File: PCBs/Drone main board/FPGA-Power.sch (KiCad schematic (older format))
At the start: 45 parts, among them U1201 10CL040_F484

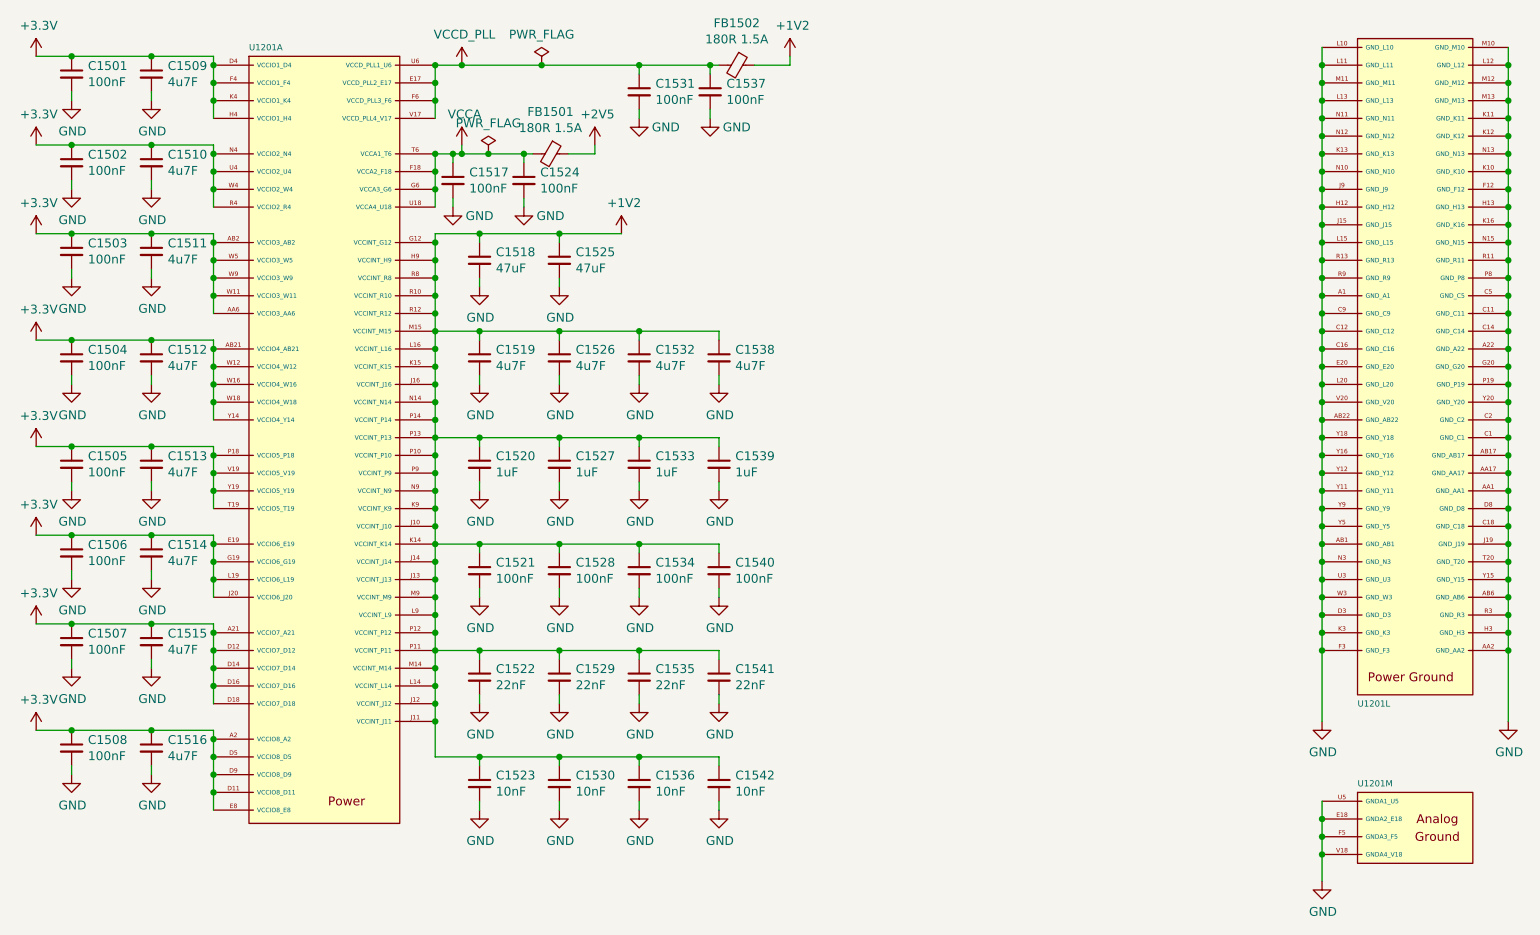
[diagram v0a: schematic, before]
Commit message: Added PDFs of schematics. Corrected a few value labels in drone schematic.
Signed-off-by: Eldalote.Electronics <Eldalote.Electronics@gmail.com>
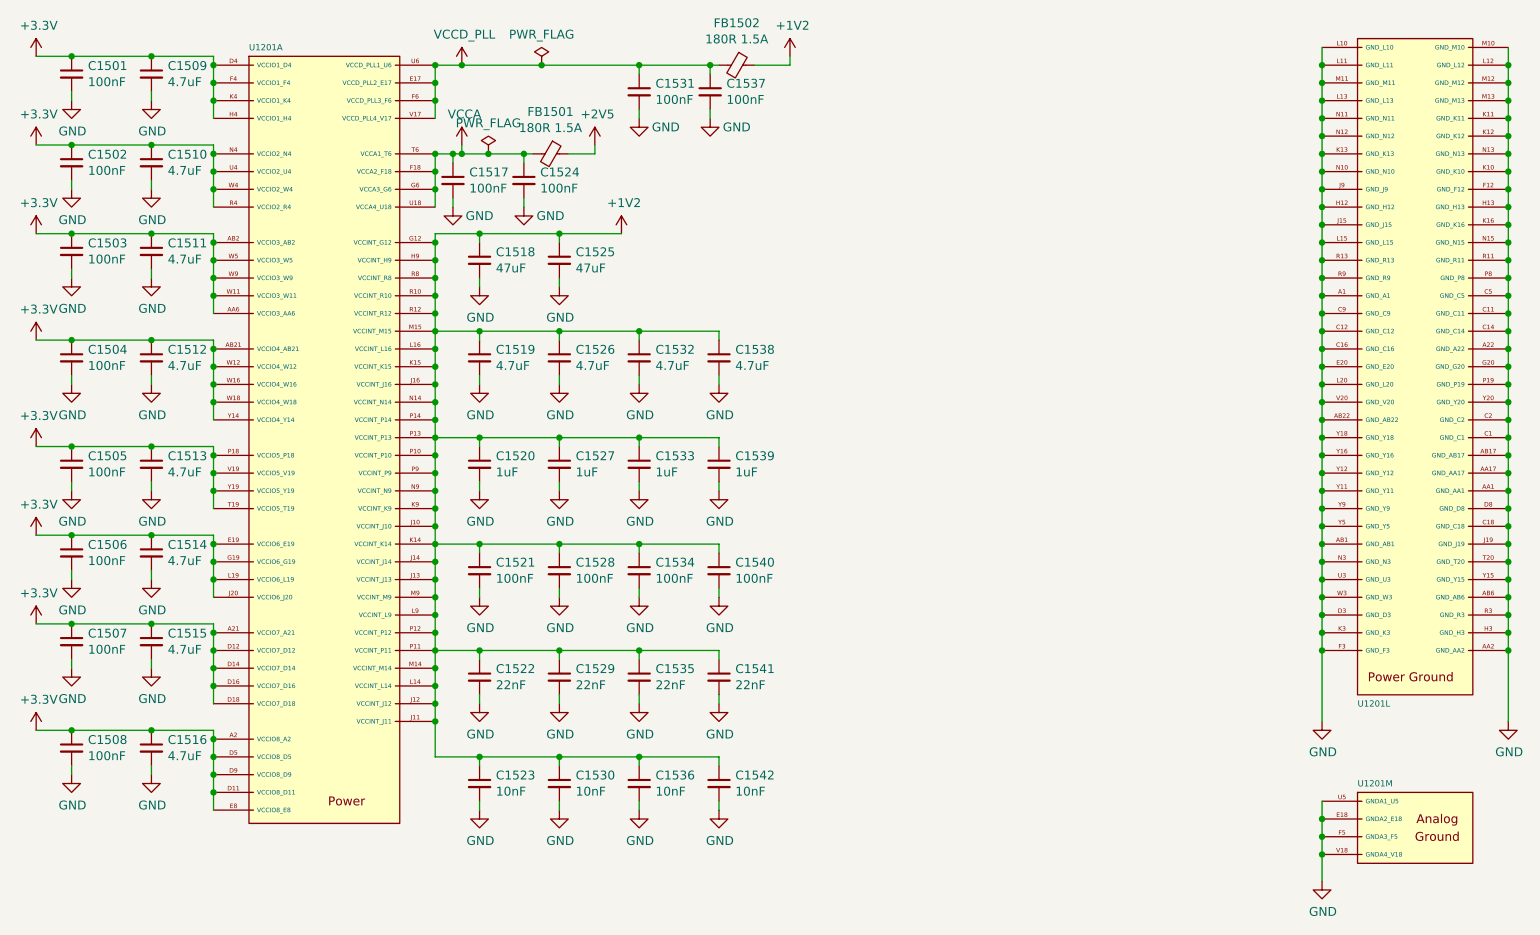
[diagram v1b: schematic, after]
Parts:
- C1509, C1510, C1511, C1512, C1513, C1514, C1515, C1516, C1519, C1526, C1532, C1538: value 4u7F -> 4.7uF
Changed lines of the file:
@@
 P 4800 2650
 F 0 "C1538" H 4892 2696 50  0000 L CNN
-F 1 "4u7F" H 4892 2605 50  0000 L CNN
+F 1 "4.7uF" H 4892 2605 50  0000 L CNN
 F 2 "Inductor_SMD:L_0402_1005Metric" H 4800 2650 50  0001 C CNN
 F 3 "~" H 4800 2650 50  0001 C CNN
@@
 P 4350 2650
 F 0 "C1532" H 4442 2696 50  0000 L CNN
-F 1 "4u7F" H 4442 2605 50  0000 L CNN
+F 1 "4.7uF" H 4442 2605 50  0000 L CNN
 F 2 "Inductor_SMD:L_0402_1005Metric" H 4350 2650 50  0001 C CNN
 F 3 "~" H 4350 2650 50  0001 C CNN
@@
 P 3900 2650
 F 0 "C1526" H 3992 2696 50  0000 L CNN
-F 1 "4u7F" H 3992 2605 50  0000 L CNN
+F 1 "4.7uF" H 3992 2605 50  0000 L CNN
 F 2 "Inductor_SMD:L_0402_1005Metric" H 3900 2650 50  0001 C CNN
 F 3 "~" H 3900 2650 50  0001 C CNN
@@
 P 3450 2650
 F 0 "C1519" H 3542 2696 50  0000 L CNN
-F 1 "4u7F" H 3542 2605 50  0000 L CNN
+F 1 "4.7uF" H 3542 2605 50  0000 L CNN
 F 2 "Inductor_SMD:L_0402_1005Metric" H 3450 2650 50  0001 C CNN
 F 3 "~" H 3450 2650 50  0001 C CNN
@@
 P 1600 2650
 F 0 "C1512" H 1692 2696 50  0000 L CNN
-F 1 "4u7F" H 1692 2605 50  0000 L CNN
+F 1 "4.7uF" H 1692 2605 50  0000 L CNN
 F 2 "Inductor_SMD:L_0402_1005Metric" H 1600 2650 50  0001 C CNN
 F 3 "~" H 1600 2650 50  0001 C CNN
@@
 P 1600 3250
 F 0 "C1513" H 1692 3296 50  0000 L CNN
-F 1 "4u7F" H 1692 3205 50  0000 L CNN
+F 1 "4.7uF" H 1692 3205 50  0000 L CNN
 F 2 "Inductor_SMD:L_0402_1005Metric" H 1600 3250 50  0001 C CNN
 F 3 "~" H 1600 3250 50  0001 C CNN
@@
 P 1600 3750
 F 0 "C1514" H 1692 3796 50  0000 L CNN
-F 1 "4u7F" H 1692 3705 50  0000 L CNN
+F 1 "4.7uF" H 1692 3705 50  0000 L CNN
 F 2 "Inductor_SMD:L_0402_1005Metric" H 1600 3750 50  0001 C CNN
 F 3 "~" H 1600 3750 50  0001 C CNN
@@
 P 1600 4250
 F 0 "C1515" H 1692 4296 50  0000 L CNN
-F 1 "4u7F" H 1692 4205 50  0000 L CNN
+F 1 "4.7uF" H 1692 4205 50  0000 L CNN
 F 2 "Inductor_SMD:L_0402_1005Metric" H 1600 4250 50  0001 C CNN
 F 3 "~" H 1600 4250 50  0001 C CNN
@@
 P 1600 4850
 F 0 "C1516" H 1692 4896 50  0000 L CNN
-F 1 "4u7F" H 1692 4805 50  0000 L CNN
+F 1 "4.7uF" H 1692 4805 50  0000 L CNN
 F 2 "Inductor_SMD:L_0402_1005Metric" H 1600 4850 50  0001 C CNN
 F 3 "~" H 1600 4850 50  0001 C CNN
@@
 P 1600 2050
 F 0 "C1511" H 1692 2096 50  0000 L CNN
-F 1 "4u7F" H 1692 2005 50  0000 L CNN
+F 1 "4.7uF" H 1692 2005 50  0000 L CNN
 F 2 "Inductor_SMD:L_0402_1005Metric" H 1600 2050 50  0001 C CNN
 F 3 "~" H 1600 2050 50  0001 C CNN
@@
 P 1600 1550
 F 0 "C1510" H 1692 1596 50  0000 L CNN
-F 1 "4u7F" H 1692 1505 50  0000 L CNN
+F 1 "4.7uF" H 1692 1505 50  0000 L CNN
 F 2 "Inductor_SMD:L_0402_1005Metric" H 1600 1550 50  0001 C CNN
 F 3 "~" H 1600 1550 50  0001 C CNN
@@
 P 1600 1050
 F 0 "C1509" H 1692 1096 50  0000 L CNN
-F 1 "4u7F" H 1692 1005 50  0000 L CNN
+F 1 "4.7uF" H 1692 1005 50  0000 L CNN
 F 2 "Inductor_SMD:L_0402_1005Metric" H 1600 1050 50  0001 C CNN
 F 3 "~" H 1600 1050 50  0001 C CNN

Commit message: Lots of work to check every component, add Manufacturers number (instead of LCSC or digikey and mouser numbers)
Changed to USB-C connector, almost done with that sheet. Components checked, need to redo Sheet IO

Signed-off-by: Eldalote.Electronics <Eldalote.Electronics@gmail.com>
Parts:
- C1501, C1502, C1503, C1504, C1505, C1506, C1507, C1508, C1517, C1521, C1524, C1528, C1531, C1534, C1537, C1540: LCSC C1525 -> (none); MfNr (none) -> CL05B104KO5NNNC
- C1509, C1510, C1511, C1512, C1513, C1514, C1515, C1516, C1519, C1526, C1532, C1538: footprint Inductor_SMD:L_0402_1005Metric -> Capacitor_SMD:C_0402_1005Metric; LCSC C23733 -> (none); MfNr (none) -> CL05A475MP5NRN
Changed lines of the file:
@@
 F 0 "C1538" H 4892 2696 50  0000 L CNN
 F 1 "4.7uF" H 4892 2605 50  0000 L CNN
-F 2 "Inductor_SMD:L_0402_1005Metric" H 4800 2650 50  0001 C CNN
+F 2 "Capacitor_SMD:C_0402_1005Metric" H 4800 2650 50  0001 C CNN
 F 3 "~" H 4800 2650 50  0001 C CNN
-F 4 "C23733" H 4800 2650 50  0001 C CNN "LCSC"
+F 4 "" H 4800 2650 50  0001 C CNN "LCSC"
+F 5 "CL05A475MP5NRN" H 4800 2650 50  0001 C CNN "MfNr"
 	1    4800 2650
 	1    0    0    -1
@@
 F 0 "C1532" H 4442 2696 50  0000 L CNN
 F 1 "4.7uF" H 4442 2605 50  0000 L CNN
-F 2 "Inductor_SMD:L_0402_1005Metric" H 4350 2650 50  0001 C CNN
+F 2 "Capacitor_SMD:C_0402_1005Metric" H 4350 2650 50  0001 C CNN
 F 3 "~" H 4350 2650 50  0001 C CNN
-F 4 "C23733" H 4350 2650 50  0001 C CNN "LCSC"
+F 4 "" H 4350 2650 50  0001 C CNN "LCSC"
+F 5 "CL05A475MP5NRN" H 4350 2650 50  0001 C CNN "MfNr"
 	1    4350 2650
 	1    0    0    -1
@@
 F 0 "C1526" H 3992 2696 50  0000 L CNN
 F 1 "4.7uF" H 3992 2605 50  0000 L CNN
-F 2 "Inductor_SMD:L_0402_1005Metric" H 3900 2650 50  0001 C CNN
+F 2 "Capacitor_SMD:C_0402_1005Metric" H 3900 2650 50  0001 C CNN
 F 3 "~" H 3900 2650 50  0001 C CNN
-F 4 "C23733" H 3900 2650 50  0001 C CNN "LCSC"
+F 4 "" H 3900 2650 50  0001 C CNN "LCSC"
+F 5 "CL05A475MP5NRN" H 3900 2650 50  0001 C CNN "MfNr"
 	1    3900 2650
 	1    0    0    -1
@@
 F 0 "C1519" H 3542 2696 50  0000 L CNN
 F 1 "4.7uF" H 3542 2605 50  0000 L CNN
-F 2 "Inductor_SMD:L_0402_1005Metric" H 3450 2650 50  0001 C CNN
+F 2 "Capacitor_SMD:C_0402_1005Metric" H 3450 2650 50  0001 C CNN
 F 3 "~" H 3450 2650 50  0001 C CNN
-F 4 "C23733" H 3450 2650 50  0001 C CNN "LCSC"
+F 4 "" H 3450 2650 50  0001 C CNN "LCSC"
+F 5 "CL05A475MP5NRN" H 3450 2650 50  0001 C CNN "MfNr"
 	1    3450 2650
 	1    0    0    -1
@@
 F 2 "Inductor_SMD:L_0402_1005Metric" H 3450 3850 50  0001 C CNN
 F 3 "~" H 3450 3850 50  0001 C CNN
-F 4 "C1525" H 3450 3850 50  0001 C CNN "LCSC"
+F 4 "" H 3450 3850 50  0001 C CNN "LCSC"
+F 5 "CL05B104KO5NNNC" H 3450 3850 50  0001 C CNN "MfNr"
 	1    3450 3850
 	1    0    0    -1
@@
 F 2 "Inductor_SMD:L_0402_1005Metric" H 3900 3850 50  0001 C CNN
 F 3 "~" H 3900 3850 50  0001 C CNN
-F 4 "C1525" H 3900 3850 50  0001 C CNN "LCSC"
+F 4 "" H 3900 3850 50  0001 C CNN "LCSC"
+F 5 "CL05B104KO5NNNC" H 3900 3850 50  0001 C CNN "MfNr"
 	1    3900 3850
 	1    0    0    -1
@@
 F 2 "Inductor_SMD:L_0402_1005Metric" H 4350 3850 50  0001 C CNN
 F 3 "~" H 4350 3850 50  0001 C CNN
-F 4 "C1525" H 4350 3850 50  0001 C CNN "LCSC"
+F 4 "" H 4350 3850 50  0001 C CNN "LCSC"
+F 5 "CL05B104KO5NNNC" H 4350 3850 50  0001 C CNN "MfNr"
 	1    4350 3850
 	1    0    0    -1
@@
 F 2 "Inductor_SMD:L_0402_1005Metric" H 4800 3850 50  0001 C CNN
 F 3 "~" H 4800 3850 50  0001 C CNN
-F 4 "C1525" H 4800 3850 50  0001 C CNN "LCSC"
+F 4 "" H 4800 3850 50  0001 C CNN "LCSC"
+F 5 "CL05B104KO5NNNC" H 4800 3850 50  0001 C CNN "MfNr"
 	1    4800 3850
 	1    0    0    -1
@@
 F 0 "C1512" H 1692 2696 50  0000 L CNN
 F 1 "4.7uF" H 1692 2605 50  0000 L CNN
-F 2 "Inductor_SMD:L_0402_1005Metric" H 1600 2650 50  0001 C CNN
+F 2 "Capacitor_SMD:C_0402_1005Metric" H 1600 2650 50  0001 C CNN
 F 3 "~" H 1600 2650 50  0001 C CNN
-F 4 "C23733" H 1600 2650 50  0001 C CNN "LCSC"
+F 4 "" H 1600 2650 50  0001 C CNN "LCSC"
+F 5 "CL05A475MP5NRN" H 1600 2650 50  0001 C CNN "MfNr"
 	1    1600 2650
 	1    0    0    -1
@@
 F 2 "Inductor_SMD:L_0402_1005Metric" H 1150 2650 50  0001 C CNN
 F 3 "~" H 1150 2650 50  0001 C CNN
-F 4 "C1525" H 1150 2650 50  0001 C CNN "LCSC"
+F 4 "" H 1150 2650 50  0001 C CNN "LCSC"
+F 5 "CL05B104KO5NNNC" H 1150 2650 50  0001 C CNN "MfNr"
 	1    1150 2650
 	1    0    0    -1
@@
 F 0 "C1513" H 1692 3296 50  0000 L CNN
 F 1 "4.7uF" H 1692 3205 50  0000 L CNN
-F 2 "Inductor_SMD:L_0402_1005Metric" H 1600 3250 50  0001 C CNN
+F 2 "Capacitor_SMD:C_0402_1005Metric" H 1600 3250 50  0001 C CNN
 F 3 "~" H 1600 3250 50  0001 C CNN
-F 4 "C23733" H 1600 3250 50  0001 C CNN "LCSC"
+F 4 "" H 1600 3250 50  0001 C CNN "LCSC"
+F 5 "CL05A475MP5NRN" H 1600 3250 50  0001 C CNN "MfNr"
 	1    1600 3250
 	1    0    0    -1
@@
 F 2 "Inductor_SMD:L_0402_1005Metric" H 1150 3250 50  0001 C CNN
 F 3 "~" H 1150 3250 50  0001 C CNN
-F 4 "C1525" H 1150 3250 50  0001 C CNN "LCSC"
+F 4 "" H 1150 3250 50  0001 C CNN "LCSC"
+F 5 "CL05B104KO5NNNC" H 1150 3250 50  0001 C CNN "MfNr"
 	1    1150 3250
 	1    0    0    -1
@@
 F 0 "C1514" H 1692 3796 50  0000 L CNN
 F 1 "4.7uF" H 1692 3705 50  0000 L CNN
-F 2 "Inductor_SMD:L_0402_1005Metric" H 1600 3750 50  0001 C CNN
+F 2 "Capacitor_SMD:C_0402_1005Metric" H 1600 3750 50  0001 C CNN
 F 3 "~" H 1600 3750 50  0001 C CNN
-F 4 "C23733" H 1600 3750 50  0001 C CNN "LCSC"
+F 4 "" H 1600 3750 50  0001 C CNN "LCSC"
+F 5 "CL05A475MP5NRN" H 1600 3750 50  0001 C CNN "MfNr"
 	1    1600 3750
 	1    0    0    -1
@@
 F 2 "Inductor_SMD:L_0402_1005Metric" H 1150 3750 50  0001 C CNN
 F 3 "~" H 1150 3750 50  0001 C CNN
-F 4 "C1525" H 1150 3750 50  0001 C CNN "LCSC"
+F 4 "" H 1150 3750 50  0001 C CNN "LCSC"
+F 5 "CL05B104KO5NNNC" H 1150 3750 50  0001 C CNN "MfNr"
 	1    1150 3750
 	1    0    0    -1
@@
 F 0 "C1515" H 1692 4296 50  0000 L CNN
 F 1 "4.7uF" H 1692 4205 50  0000 L CNN
-F 2 "Inductor_SMD:L_0402_1005Metric" H 1600 4250 50  0001 C CNN
+F 2 "Capacitor_SMD:C_0402_1005Metric" H 1600 4250 50  0001 C CNN
 F 3 "~" H 1600 4250 50  0001 C CNN
-F 4 "C23733" H 1600 4250 50  0001 C CNN "LCSC"
+F 4 "" H 1600 4250 50  0001 C CNN "LCSC"
+F 5 "CL05A475MP5NRN" H 1600 4250 50  0001 C CNN "MfNr"
 	1    1600 4250
 	1    0    0    -1
@@
 F 2 "Inductor_SMD:L_0402_1005Metric" H 1150 4250 50  0001 C CNN
 F 3 "~" H 1150 4250 50  0001 C CNN
-F 4 "C1525" H 1150 4250 50  0001 C CNN "LCSC"
+F 4 "" H 1150 4250 50  0001 C CNN "LCSC"
+F 5 "CL05B104KO5NNNC" H 1150 4250 50  0001 C CNN "MfNr"
 	1    1150 4250
 	1    0    0    -1
@@
 F 0 "C1516" H 1692 4896 50  0000 L CNN
 F 1 "4.7uF" H 1692 4805 50  0000 L CNN
-F 2 "Inductor_SMD:L_0402_1005Metric" H 1600 4850 50  0001 C CNN
+F 2 "Capacitor_SMD:C_0402_1005Metric" H 1600 4850 50  0001 C CNN
 F 3 "~" H 1600 4850 50  0001 C CNN
-F 4 "C23733" H 1600 4850 50  0001 C CNN "LCSC"
+F 4 "" H 1600 4850 50  0001 C CNN "LCSC"
+F 5 "CL05A475MP5NRN" H 1600 4850 50  0001 C CNN "MfNr"
 	1    1600 4850
 	1    0    0    -1
@@
 F 2 "Inductor_SMD:L_0402_1005Metric" H 1150 4850 50  0001 C CNN
 F 3 "~" H 1150 4850 50  0001 C CNN
-F 4 "C1525" H 1150 4850 50  0001 C CNN "LCSC"
+F 4 "" H 1150 4850 50  0001 C CNN "LCSC"
+F 5 "CL05B104KO5NNNC" H 1150 4850 50  0001 C CNN "MfNr"
 	1    1150 4850
 	1    0    0    -1
@@
 F 2 "Inductor_SMD:L_0402_1005Metric" H 1150 2050 50  0001 C CNN
 F 3 "~" H 1150 2050 50  0001 C CNN
-F 4 "C1525" H 1150 2050 50  0001 C CNN "LCSC"
+F 4 "" H 1150 2050 50  0001 C CNN "LCSC"
+F 5 "CL05B104KO5NNNC" H 1150 2050 50  0001 C CNN "MfNr"
 	1    1150 2050
 	1    0    0    -1
@@
 F 0 "C1511" H 1692 2096 50  0000 L CNN
 F 1 "4.7uF" H 1692 2005 50  0000 L CNN
-F 2 "Inductor_SMD:L_0402_1005Metric" H 1600 2050 50  0001 C CNN
+F 2 "Capacitor_SMD:C_0402_1005Metric" H 1600 2050 50  0001 C CNN
 F 3 "~" H 1600 2050 50  0001 C CNN
-F 4 "C23733" H 1600 2050 50  0001 C CNN "LCSC"
+F 4 "" H 1600 2050 50  0001 C CNN "LCSC"
+F 5 "CL05A475MP5NRN" H 1600 2050 50  0001 C CNN "MfNr"
 	1    1600 2050
 	1    0    0    -1
@@
 F 2 "Inductor_SMD:L_0402_1005Metric" H 1150 1550 50  0001 C CNN
 F 3 "~" H 1150 1550 50  0001 C CNN
-F 4 "C1525" H 1150 1550 50  0001 C CNN "LCSC"
+F 4 "" H 1150 1550 50  0001 C CNN "LCSC"
+F 5 "CL05B104KO5NNNC" H 1150 1550 50  0001 C CNN "MfNr"
 	1    1150 1550
 	1    0    0    -1
@@
 F 0 "C1510" H 1692 1596 50  0000 L CNN
 F 1 "4.7uF" H 1692 1505 50  0000 L CNN
-F 2 "Inductor_SMD:L_0402_1005Metric" H 1600 1550 50  0001 C CNN
+F 2 "Capacitor_SMD:C_0402_1005Metric" H 1600 1550 50  0001 C CNN
 F 3 "~" H 1600 1550 50  0001 C CNN
-F 4 "C23733" H 1600 1550 50  0001 C CNN "LCSC"
+F 4 "" H 1600 1550 50  0001 C CNN "LCSC"
+F 5 "CL05A475MP5NRN" H 1600 1550 50  0001 C CNN "MfNr"
 	1    1600 1550
 	1    0    0    -1
@@
 F 2 "Inductor_SMD:L_0402_1005Metric" H 1150 1050 50  0001 C CNN
 F 3 "~" H 1150 1050 50  0001 C CNN
-F 4 "C1525" H 1150 1050 50  0001 C CNN "LCSC"
+F 4 "" H 1150 1050 50  0001 C CNN "LCSC"
+F 5 "CL05B104KO5NNNC" H 1150 1050 50  0001 C CNN "MfNr"
 	1    1150 1050
 	1    0    0    -1
@@
 F 0 "C1509" H 1692 1096 50  0000 L CNN
 F 1 "4.7uF" H 1692 1005 50  0000 L CNN
-F 2 "Inductor_SMD:L_0402_1005Metric" H 1600 1050 50  0001 C CNN
+F 2 "Capacitor_SMD:C_0402_1005Metric" H 1600 1050 50  0001 C CNN
 F 3 "~" H 1600 1050 50  0001 C CNN
-F 4 "C23733" H 1600 1050 50  0001 C CNN "LCSC"
+F 4 "" H 1600 1050 50  0001 C CNN "LCSC"
+F 5 "CL05A475MP5NRN" H 1600 1050 50  0001 C CNN "MfNr"
 	1    1600 1050
 	1    0    0    -1
@@
 F 2 "Capacitor_SMD:C_0402_1005Metric" H 3300 1650 50  0001 C CNN
 F 3 "~" H 3300 1650 50  0001 C CNN
-F 4 "C1525" H 3300 1650 50  0001 C CNN "LCSC"
+F 4 "" H 3300 1650 50  0001 C CNN "LCSC"
+F 5 "CL05B104KO5NNNC" H 3300 1650 50  0001 C CNN "MfNr"
 	1    3300 1650
 	1    0    0    -1
@@
 F 2 "Capacitor_SMD:C_0402_1005Metric" H 3700 1650 50  0001 C CNN
 F 3 "~" H 3700 1650 50  0001 C CNN
-F 4 "C1525" H 3700 1650 50  0001 C CNN "LCSC"
+F 4 "" H 3700 1650 50  0001 C CNN "LCSC"
+F 5 "CL05B104KO5NNNC" H 3700 1650 50  0001 C CNN "MfNr"
 	1    3700 1650
 	1    0    0    -1
@@
 F 2 "Capacitor_SMD:C_0402_1005Metric" H 4750 1150 50  0001 C CNN
 F 3 "~" H 4750 1150 50  0001 C CNN
-F 4 "C1525" H 4750 1150 50  0001 C CNN "LCSC"
+F 4 "" H 4750 1150 50  0001 C CNN "LCSC"
+F 5 "CL05B104KO5NNNC" H 4750 1150 50  0001 C CNN "MfNr"
 	1    4750 1150
 	1    0    0    -1
@@
 F 2 "Capacitor_SMD:C_0402_1005Metric" H 4350 1150 50  0001 C CNN
 F 3 "~" H 4350 1150 50  0001 C CNN
-F 4 "C1525" H 4350 1150 50  0001 C CNN "LCSC"
+F 4 "" H 4350 1150 50  0001 C CNN "LCSC"
+F 5 "CL05B104KO5NNNC" H 4350 1150 50  0001 C CNN "MfNr"
 	1    4350 1150
 	1    0    0    -1

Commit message: Finished (?) the schematic check and update. Next: PCB update
Signed-off-by: Eldalote.Electronics <Eldalote.Electronics@gmail.com>
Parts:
- C1518, C1525: DigiKey 1276-3036-1-ND -> (none); MfNr (none) -> CL21A476MQYNNN; Mouser 187-CL21X476MRYNNNE -> (none)
- C1520, C1527, C1533, C1539: LCSC C52923 -> (none); MfNr (none) -> CL05A105KA5NQN
- C1522, C1529, C1535, C1541: LCSC C1532 -> (none); MfNr (none) -> CL05B223KA5NNN
- C1523, C1530, C1536, C1542: LCSC C15195 -> (none); MfNr (none) -> CL05B103KB5NNN
- FB1501, FB1502: footprint Inductor_SMD:L_0603_1608Metric_Pad1.05x0.95mm_HandSolder -> Inductor_SMD:L_0603_1608Metric; DigiKey 490-5263-1-ND -> (none); MfNr (none) -> MPZ1608S181ATAH0; Mouser 81-BLM18PG181SN1D -> (none)
- U1201: MfNr (none) -> 10CL040Y
